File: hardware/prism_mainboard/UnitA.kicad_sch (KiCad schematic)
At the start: 3 parts, among them U1 XC7Z010-1CLG400C

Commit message: Zynq-7000 Schematic Updates
Added basic power net labels for the PL and PS portions of the FPGA.
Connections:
- net GND: now reaches U1.A8 (GND)
- net GND: now also U1.B1 (GND), U1.C4 (GND), U1.C9 (GND), U1.F3 (GND), U1.F7 (GND), U1.H7 (GND), U1.H9 (GND), U1.J2 (GND), U1.J8 (GND), U1.K5 (GND), U1.K7 (GND), U1.L8 (GND), U1.M1 (GND)
- net VCCPAUX: now reaches U1.F8 (VCCPAUX)
- net VCCPAUX: now also U1.G9 (VCCPAUX), U1.K8 (VCCPAUX)
- net VCCPLL: now reaches U1.G8 (VCCPLL)

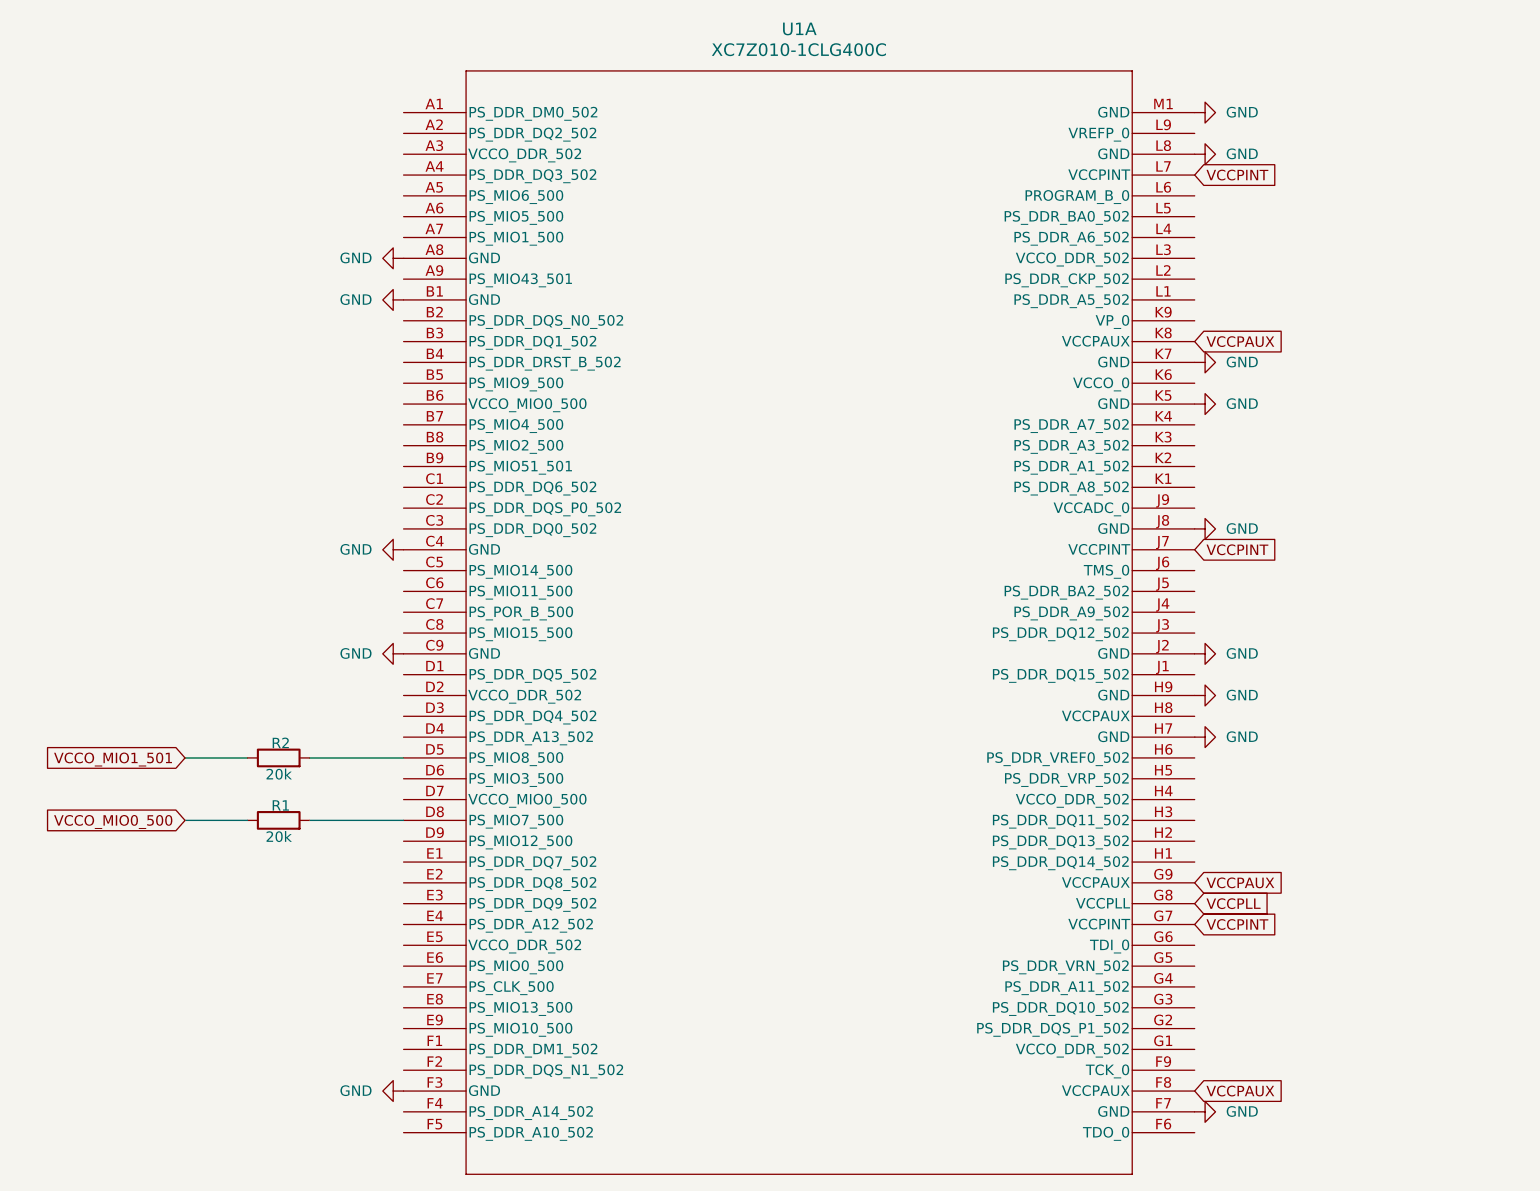
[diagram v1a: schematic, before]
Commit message: Mainboard Updates
Started a lot of the basic schematic nets like GND and Power nets. Major Change: Decided on using the XC7Z015-1CLG485I instead of the 7010 or 7020 due to the ability to use HDMI interfaces with an adapter and more LUTs. Updated schematic symbols and footprints accordingly. Added Memory, Encoder, MicroSD schematics. Added LimeSDR footprints as well. Will Try to add Power to the entire board next.
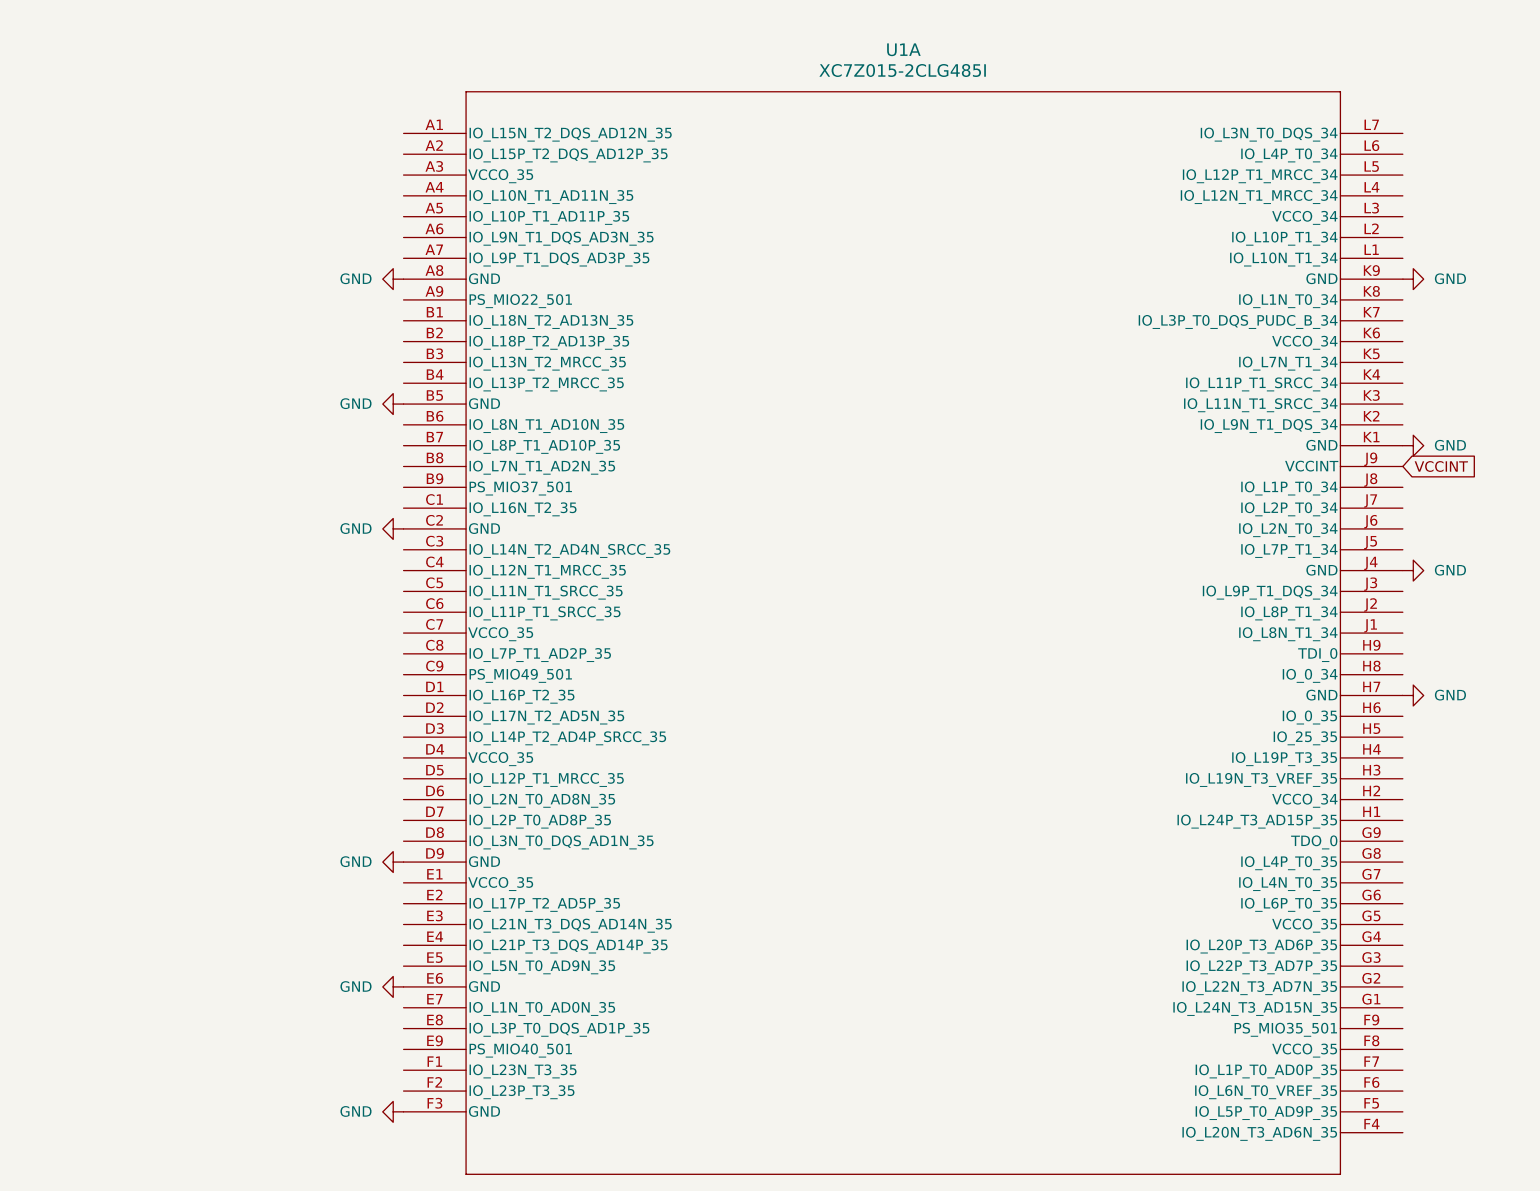
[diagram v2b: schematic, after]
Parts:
- removed R1, R2: 20k, symbol Device:R
- removed U1: XC7Z010-1CLG400C, XC7Z010-1CLG400C:CLG400_XIL, symbol XC7Z010-1CLG400C:XC7Z010-1CLG400C
- added U1: XC7Z015-2CLG485I, CLG485_XIL, symbol XC7Z015-CLG485:XC7Z015-2CLG485I
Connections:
- net GND: now also U1.A8 (GND), U1.B5 (GND), U1.C2 (GND), U1.D9 (GND), U1.E6 (GND), U1.F3 (GND), U1.H7 (GND), U1.J4 (GND), U1.K1 (GND), U1.K9 (GND)
- new net VCCINT: U1.J9 (VCCINT)

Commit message: Schematic Updates
Updated the DDR3 DRAM to 4Gb, added a lot of nets and started updating the power and decoupling components. Updated .gitignore to avoid .mkv files.
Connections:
- net VCCO_35: now reaches U1.A3 (VCCO_35)
- net VCCO_35: now also U1.C7 (VCCO_35), U1.D4 (VCCO_35), U1.E1 (VCCO_35), U1.F8 (VCCO_35), U1.G5 (VCCO_35)
- net VCCO_34: now reaches U1.H2 (VCCO_34)
- net VCCO_34: now also U1.K6 (VCCO_34), U1.L3 (VCCO_34)
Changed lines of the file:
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@@
 	(generator_version "10.0")
 	(paper "A4")
+	(global_label "VCCO_35"
+		(shape input)
+		(at 81.28 120.65 180)
+		(fields_autoplaced yes)
+		(effects
+			(font
+				(size 1.27 1.27)
+			)
+			(justify right)
+		)
+		(property "Intersheetrefs" "${INTERSHEET_REFS}"
+			(at 69.9491 120.65 0)
+			(hide yes)
+			(show_name no)
+			(do_not_autoplace no)
+			(effects
+				(font
+					(size 1.27 1.27)
+				)
+				(justify right)
+			)
+		)
+	)
+	(global_label "VCCO_34"
+		(shape input)
+		(at 203.2 54.61 0)
+		(fields_autoplaced yes)
+		(effects
+			(font
+				(size 1.27 1.27)
+			)
+			(justify left)
+		)
+		(property "Intersheetrefs" "${INTERSHEET_REFS}"
+			(at 214.5309 54.61 0)
+			(hide yes)
+			(show_name no)
+			(do_not_autoplace no)
+			(effects
+				(font
+					(size 1.27 1.27)
+				)
+				(justify left)
+			)
+		)
+	)
+	(global_label "VCCO_35"
+		(shape input)
+		(at 81.28 105.41 180)
+		(fields_autoplaced yes)
+		(effects
+			(font
+				(size 1.27 1.27)
+			)
+			(justify right)
+		)
+		(property "Intersheetrefs" "${INTERSHEET_REFS}"
+			(at 69.9491 105.41 0)
+			(hide yes)
+			(show_name no)
+			(do_not_autoplace no)
+			(effects
+				(font
+					(size 1.27 1.27)
+				)
+				(justify right)
+			)
+		)
+	)
+	(global_label "VCCO_34"
+		(shape input)
+		(at 203.2 39.37 0)
+		(fields_autoplaced yes)
+		(effects
+			(font
+				(size 1.27 1.27)
+			)
+			(justify left)
+		)
+		(property "Intersheetrefs" "${INTERSHEET_REFS}"
+			(at 214.5309 39.37 0)
+			(hide yes)
+			(show_name no)
+			(do_not_autoplace no)
+			(effects
+				(font
+					(size 1.27 1.27)
+				)
+				(justify left)
+			)
+		)
+	)
+	(global_label "VCCO_35"
+		(shape input)
+		(at 203.2 140.97 0)
+		(fields_autoplaced yes)
+		(effects
+			(font
+				(size 1.27 1.27)
+			)
+			(justify left)
+		)
+		(property "Intersheetrefs" "${INTERSHEET_REFS}"
+			(at 214.5309 140.97 0)
+			(hide yes)
+			(show_name no)
+			(do_not_autoplace no)
+			(effects
+				(font
+					(size 1.27 1.27)
+				)
+				(justify left)
+			)
+		)
+	)
 	(global_label "VCCINT"
 		(shape input)
@@
 			(hide yes)
 			(show_name no)
+			(do_not_autoplace no)
+			(effects
+				(font
+					(size 1.27 1.27)
+				)
+				(justify left)
+			)
+		)
+	)
+	(global_label "VCCO_34"
+		(shape input)
+		(at 203.2 110.49 0)
+		(fields_autoplaced yes)
+		(effects
+			(font
+				(size 1.27 1.27)
+			)
+			(justify left)
+		)
+		(property "Intersheetrefs" "${INTERSHEET_REFS}"
+			(at 214.5309 110.49 0)
+			(hide yes)
+			(show_name no)
+			(do_not_autoplace no)
+			(effects
+				(font
+					(size 1.27 1.27)
+				)
+				(justify left)
+			)
+		)
+	)
+	(global_label "VCCO_35"
+		(shape input)
+		(at 81.28 90.17 180)
+		(fields_autoplaced yes)
+		(effects
+			(font
+				(size 1.27 1.27)
+			)
+			(justify right)
+		)
+		(property "Intersheetrefs" "${INTERSHEET_REFS}"
+			(at 69.9491 90.17 0)
+			(hide yes)
+			(show_name no)
+			(do_not_autoplace no)
+			(effects
+				(font
+					(size 1.27 1.27)
+				)
+				(justify right)
+			)
+		)
+	)
+	(global_label "VCCO_35"
+		(shape input)
+		(at 81.28 34.29 180)
+		(fields_autoplaced yes)
+		(effects
+			(font
+				(size 1.27 1.27)
+			)
+			(justify right)
+		)
+		(property "Intersheetrefs" "${INTERSHEET_REFS}"
+			(at 69.9491 34.29 0)
+			(hide yes)
+			(show_name no)
+			(do_not_autoplace no)
+			(effects
+				(font
+					(size 1.27 1.27)
+				)
+				(justify right)
+			)
+		)
+	)
+	(global_label "VCCO_35"
+		(shape input)
+		(at 203.2 125.73 0)
+		(fields_autoplaced yes)
+		(effects
+			(font
+				(size 1.27 1.27)
+			)
+			(justify left)
+		)
+		(property "Intersheetrefs" "${INTERSHEET_REFS}"
+			(at 214.5309 125.73 0)
+			(hide yes)
+			(show_name no)

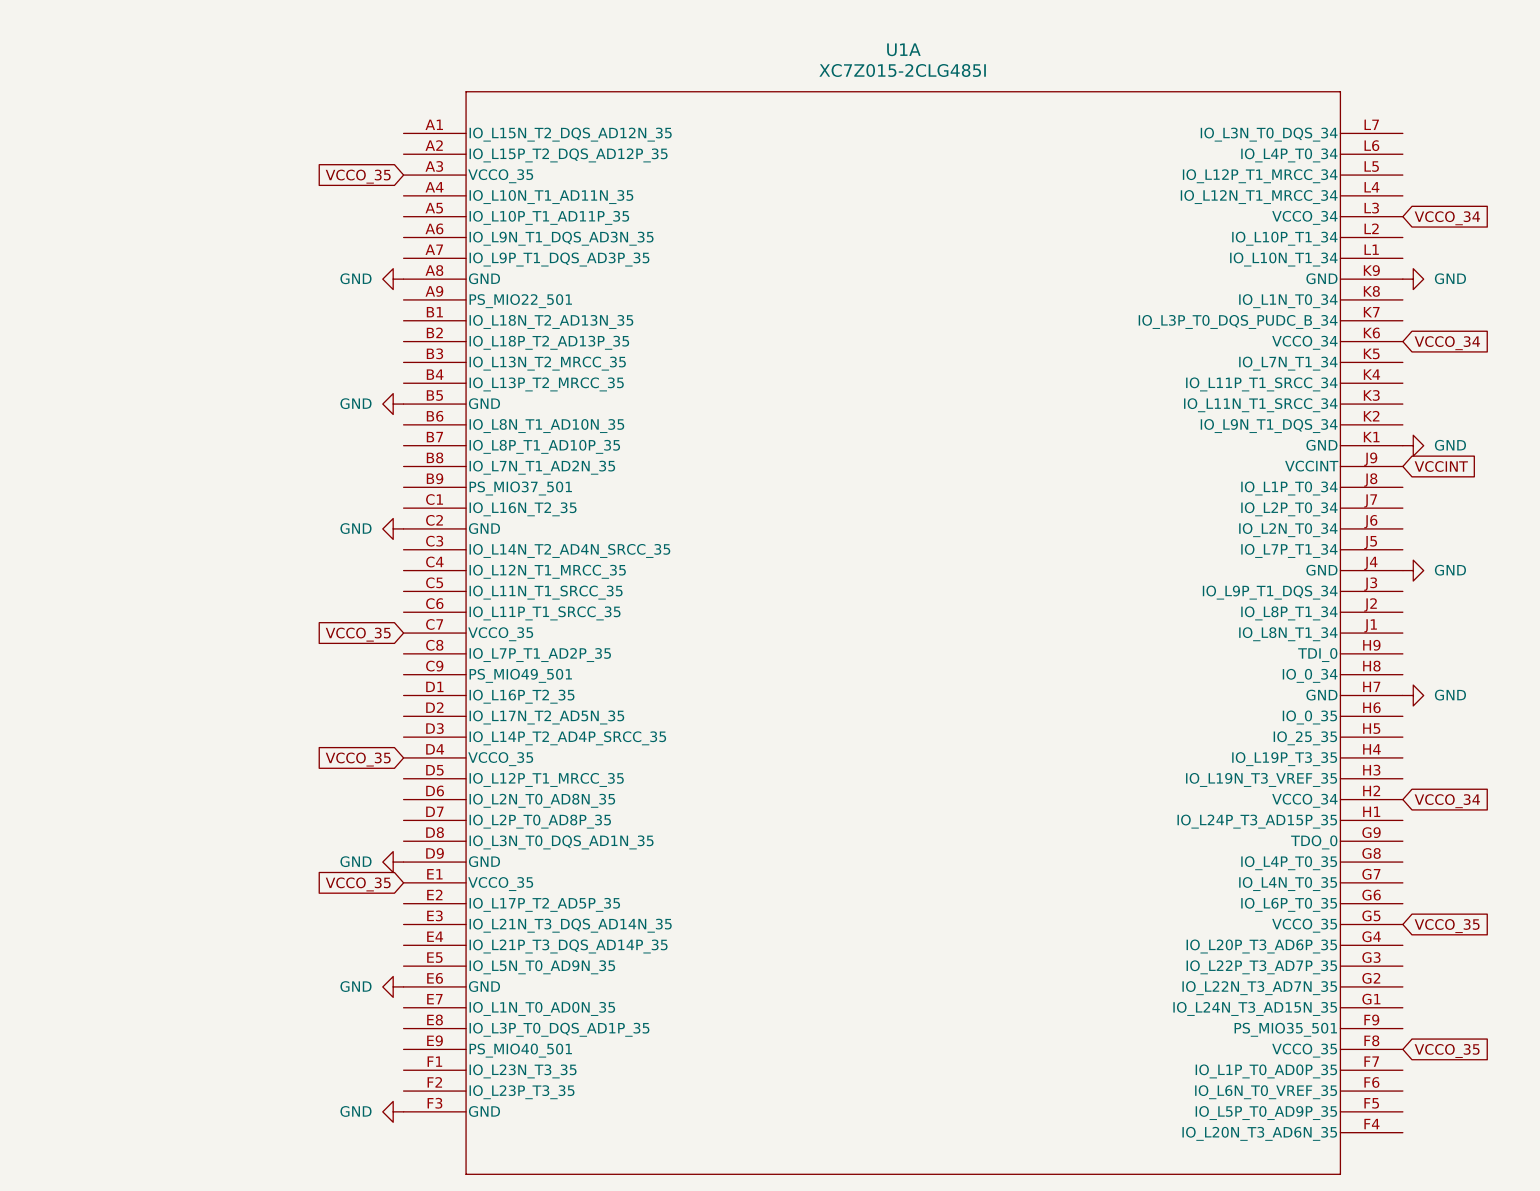
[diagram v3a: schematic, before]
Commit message: Schematic Updates
Added the LMS7002M to XC7Z015 connections, atleast the preliminary data connections.
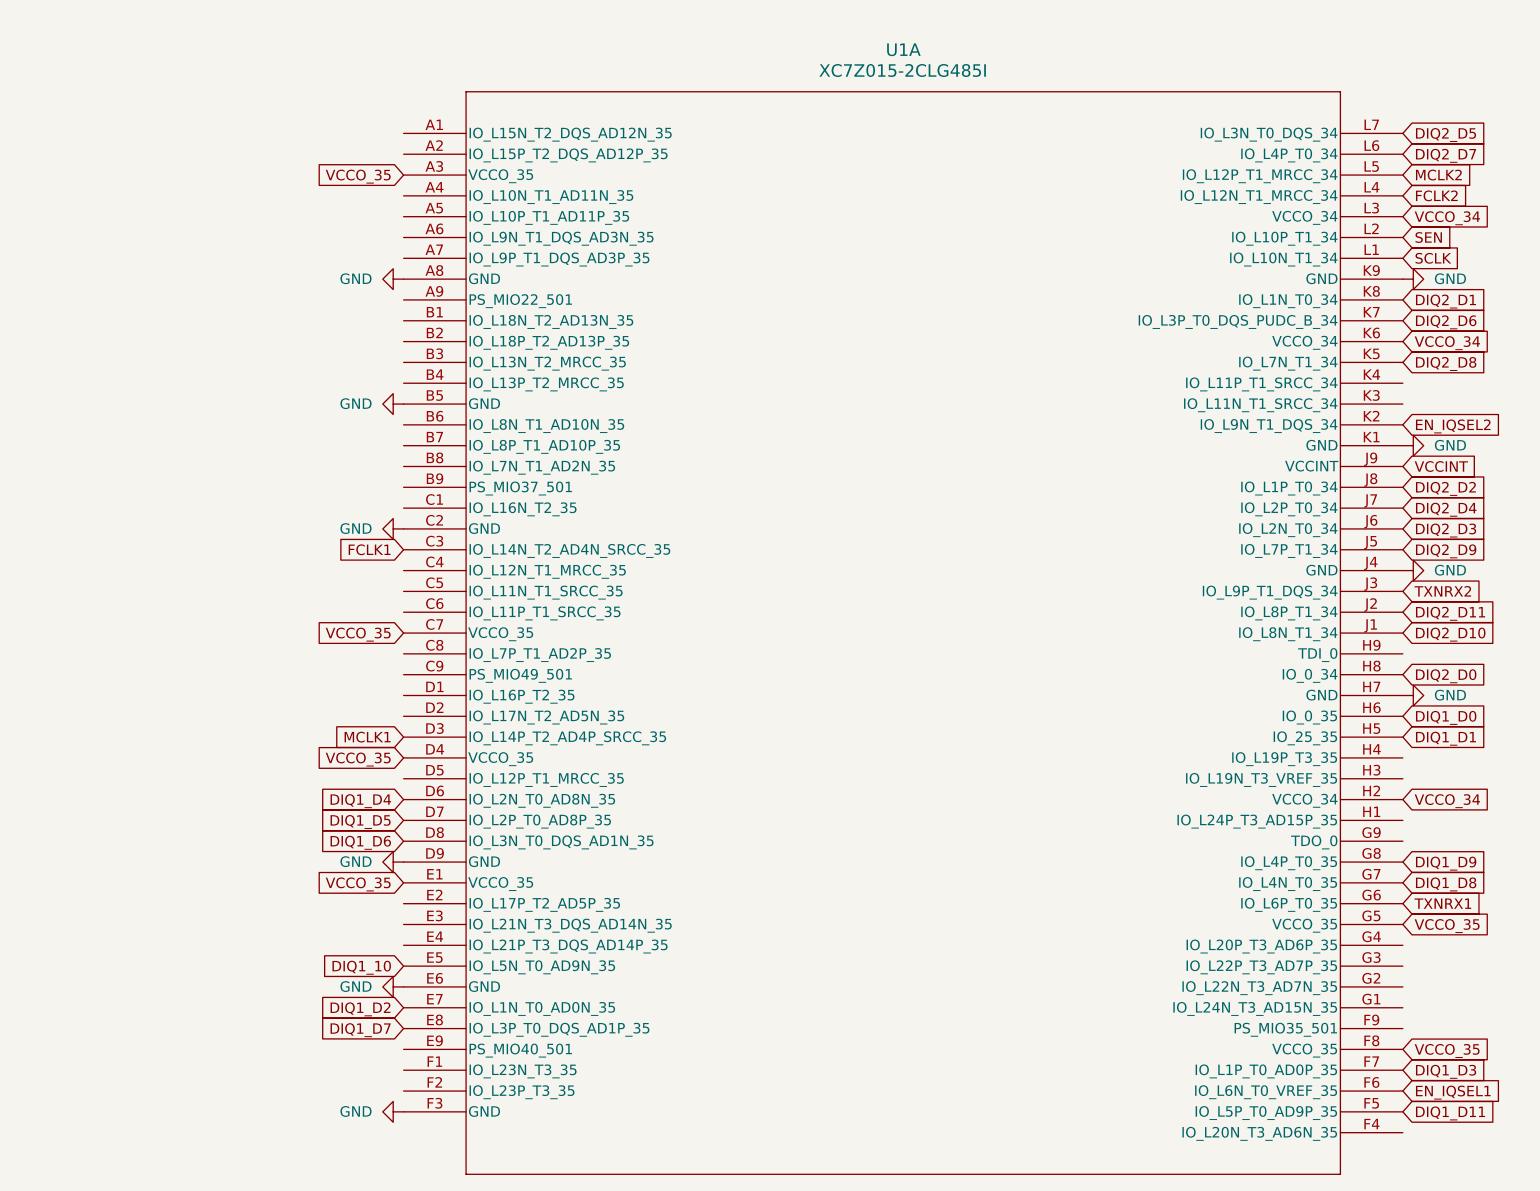
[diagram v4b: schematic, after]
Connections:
- net FCLK1: now reaches U1.C3 (IO_L14N_T2_AD4N_SRCC_35)
- net MCLK1: now reaches U1.D3 (IO_L14P_T2_AD4P_SRCC_35)
- net DIQ1_D4: now reaches U1.D6 (IO_L2N_T0_AD8N_35)
- net DIQ1_D5: now reaches U1.D7 (IO_L2P_T0_AD8P_35)
- net DIQ1_D6: now reaches U1.D8 (IO_L3N_T0_DQS_AD1N_35)
- net DIQ1_10: now reaches U1.E5 (IO_L5N_T0_AD9N_35)
- net DIQ1_D2: now reaches U1.E7 (IO_L1N_T0_AD0N_35)
- net DIQ1_D7: now reaches U1.E8 (IO_L3P_T0_DQS_AD1P_35)
- net DIQ1_D11: now reaches U1.F5 (IO_L5P_T0_AD9P_35)
- net EN_IQSEL1: now reaches U1.F6 (IO_L6N_T0_VREF_35)
- net DIQ1_D3: now reaches U1.F7 (IO_L1P_T0_AD0P_35)
- net TXNRX1: now reaches U1.G6 (IO_L6P_T0_35)
- net DIQ1_D8: now reaches U1.G7 (IO_L4N_T0_35)
- net DIQ1_D9: now reaches U1.G8 (IO_L4P_T0_35)
- net DIQ1_D1: now reaches U1.H5 (IO_25_35)
- net DIQ1_D0: now reaches U1.H6 (IO_0_35)
- net DIQ2_D0: now reaches U1.H8 (IO_0_34)
- net DIQ2_D10: now reaches U1.J1 (IO_L8N_T1_34)
- net DIQ2_D11: now reaches U1.J2 (IO_L8P_T1_34)
- net TXNRX2: now reaches U1.J3 (IO_L9P_T1_DQS_34)
- net DIQ2_D9: now reaches U1.J5 (IO_L7P_T1_34)
- net DIQ2_D3: now reaches U1.J6 (IO_L2N_T0_34)
- net DIQ2_D4: now reaches U1.J7 (IO_L2P_T0_34)
- net DIQ2_D2: now reaches U1.J8 (IO_L1P_T0_34)
- net EN_IQSEL2: now reaches U1.K2 (IO_L9N_T1_DQS_34)
- net DIQ2_D8: now reaches U1.K5 (IO_L7N_T1_34)
- net DIQ2_D6: now reaches U1.K7 (IO_L3P_T0_DQS_PUDC_B_34)
- net DIQ2_D1: now reaches U1.K8 (IO_L1N_T0_34)
- net SCLK: now reaches U1.L1 (IO_L10N_T1_34)
- net SEN: now reaches U1.L2 (IO_L10P_T1_34)
- net FCLK2: now reaches U1.L4 (IO_L12N_T1_MRCC_34)
- net MCLK2: now reaches U1.L5 (IO_L12P_T1_MRCC_34)
- net DIQ2_D7: now reaches U1.L6 (IO_L4P_T0_34)
- net DIQ2_D5: now reaches U1.L7 (IO_L3N_T0_DQS_34)
